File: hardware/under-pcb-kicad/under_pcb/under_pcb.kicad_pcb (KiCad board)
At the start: 2 copper layers, 90 x 160.1 mm, 7 parts, among them J1 Conn_01x08, J2 Conn_01x08, J3 Conn_01x08, J4 Conn_01x06, J5 Conn_02x18_Odd_Even, J6 Conn_01x08, J7 Conn_01x04

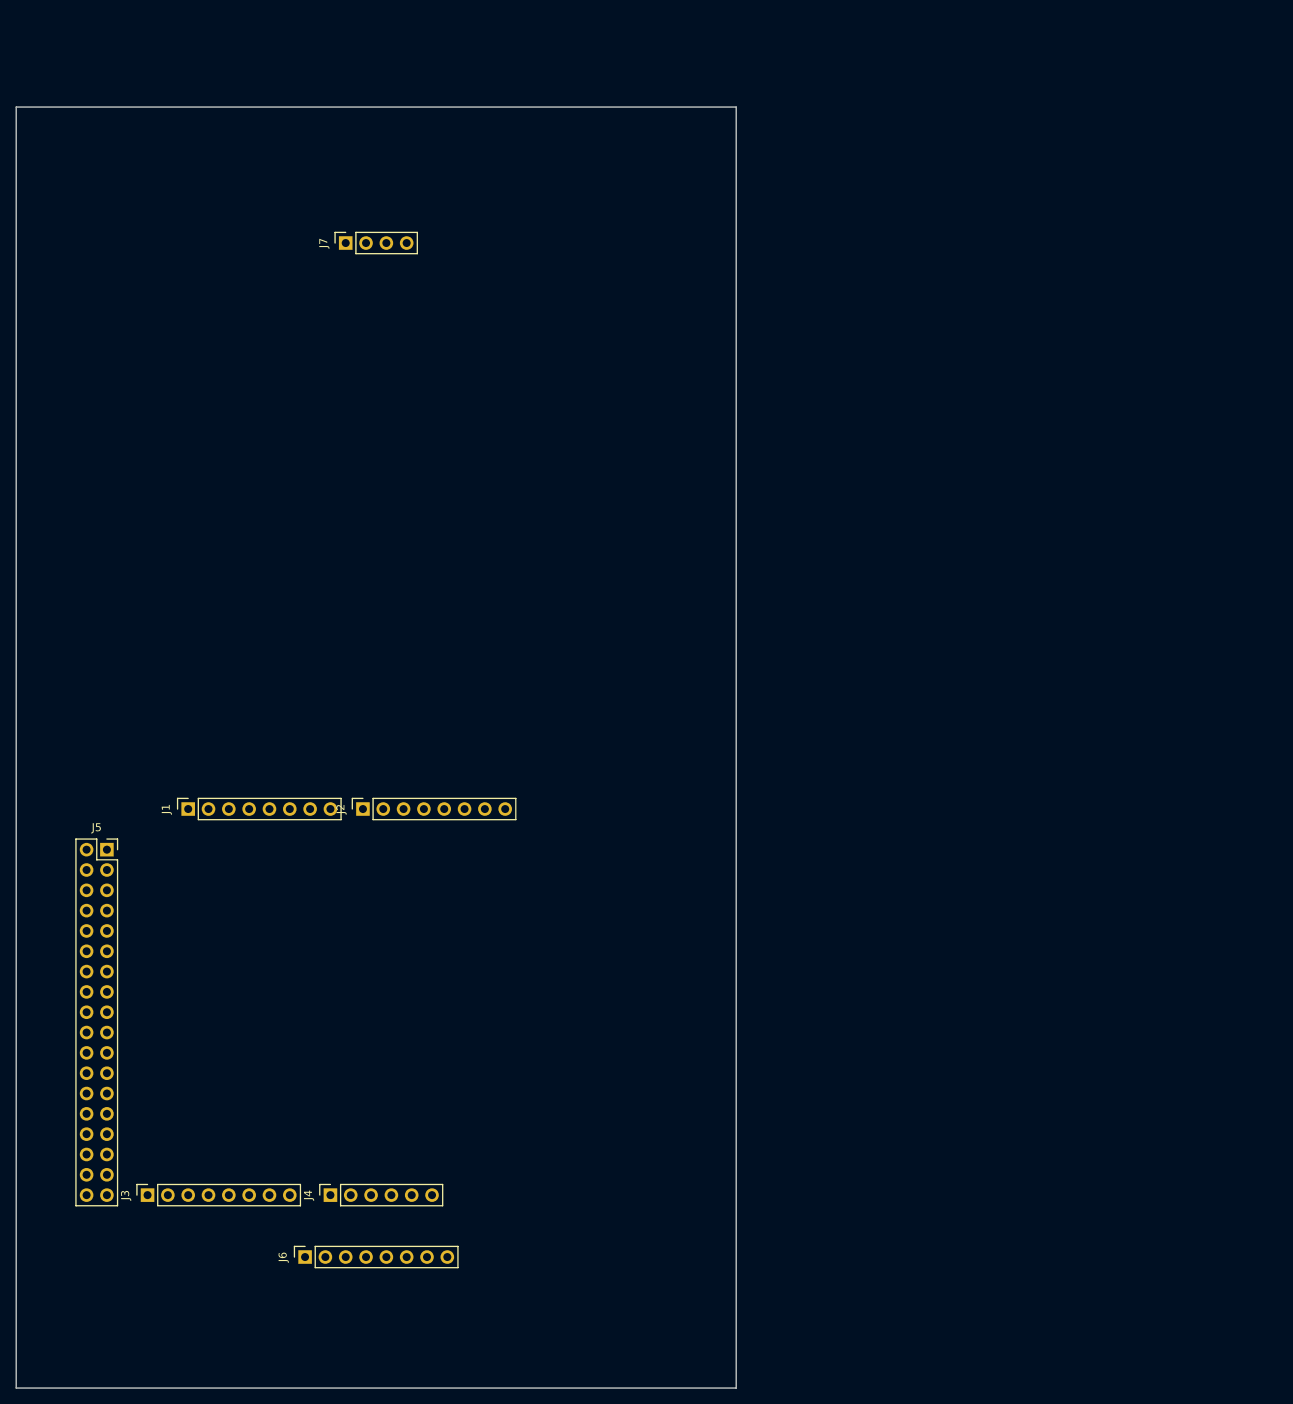
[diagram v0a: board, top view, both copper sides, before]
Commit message: wiring and routing under pcb
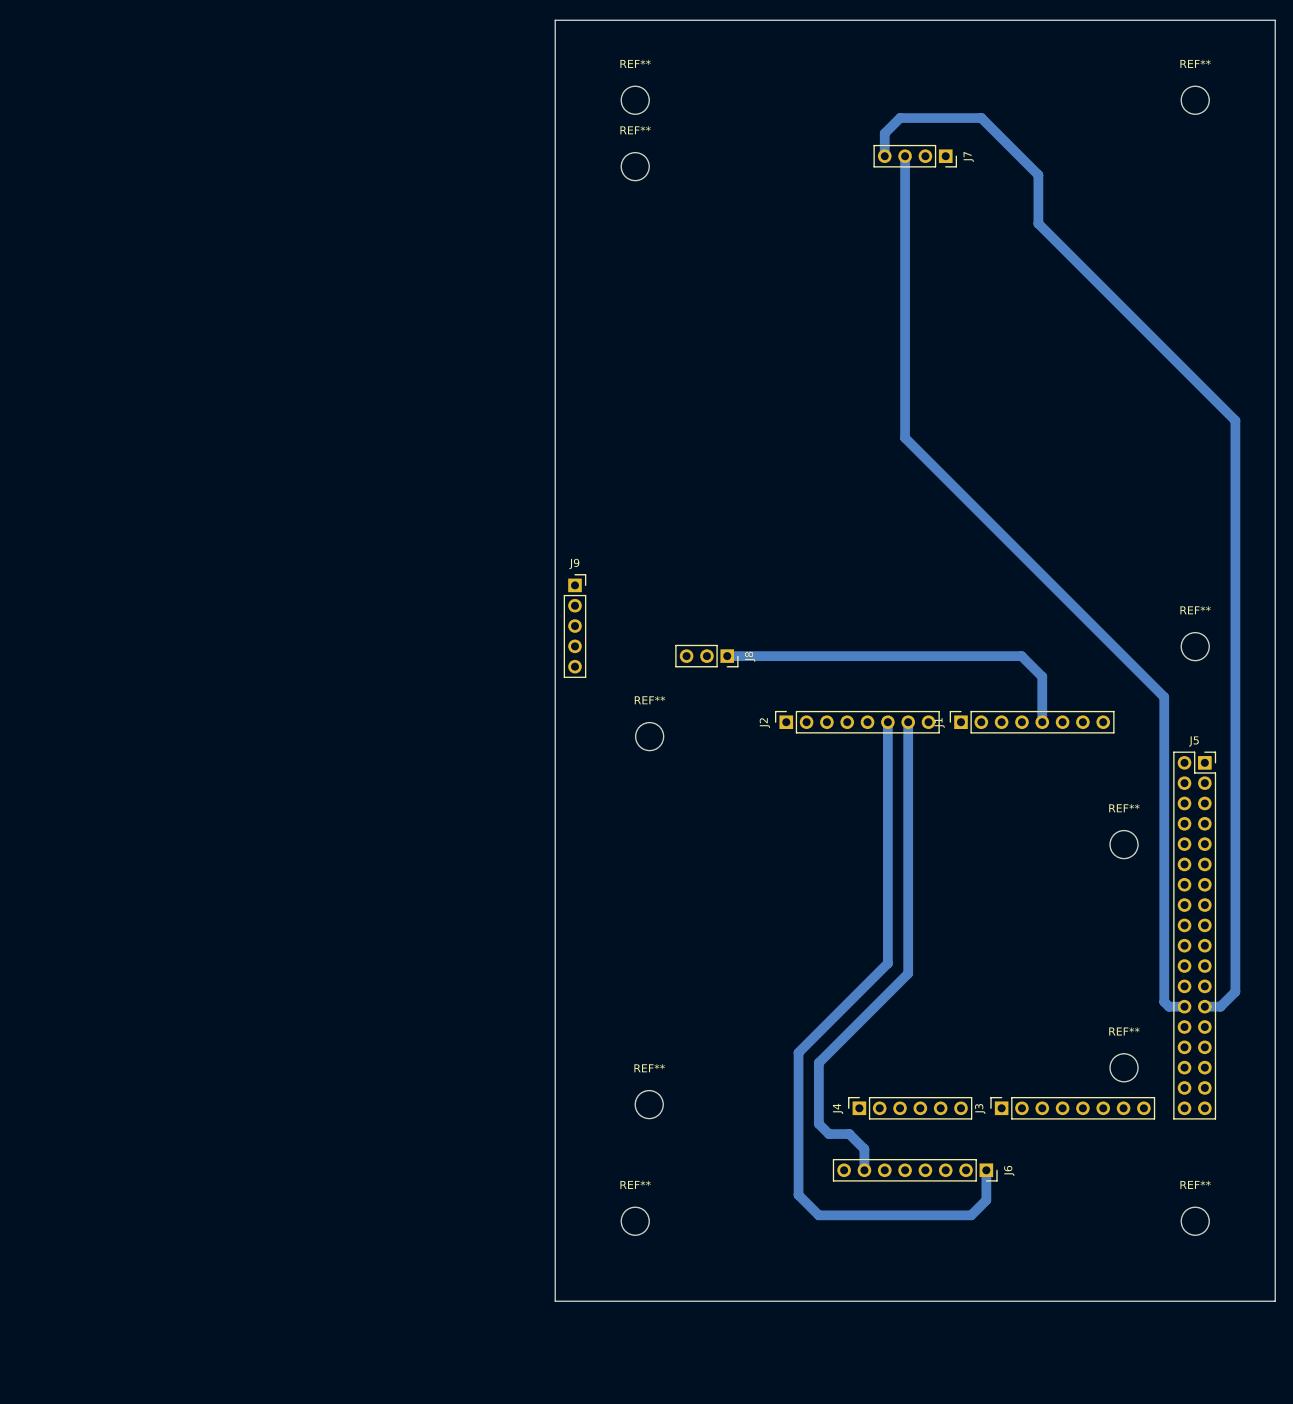
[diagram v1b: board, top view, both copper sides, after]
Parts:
- added J8: Conn_01x03, Connector_PinSocket_2.54mm:PinSocket_1x03_P2.54mm_Vertical, F.Cu at (103.9, 103.5)
- added J9: Conn_01x05, Connector_PinSocket_2.54mm:PinSocket_1x05_P2.54mm_Vertical, F.Cu at (84.8, 94.7)
- added REF**: MountingHole_3.5mm, MountingHole:MountingHole_3.5mm, F.Cu at (162.4, 34.0)
- added REF**: MountingHole_3.5mm, MountingHole:MountingHole_3.5mm, F.Cu at (92.4, 34.0)
- added REF**: MountingHole_3.5mm, MountingHole:MountingHole_3.5mm, F.Cu at (162.4, 174.2)
- added REF**: MountingHole_3.5mm, MountingHole:MountingHole_3.5mm, F.Cu at (92.4, 174.2)
- added REF**: MountingHole_3.5mm, MountingHole:MountingHole_3.5mm, F.Cu at (94.1, 159.6)
- added REF**: MountingHole_3.5mm, MountingHole:MountingHole_3.5mm, F.Cu at (153.5, 155.0)
- added REF**: MountingHole_3.5mm, MountingHole:MountingHole_3.5mm, F.Cu at (153.5, 127.1)
- added REF**: MountingHole_3.5mm, MountingHole:MountingHole_3.5mm, F.Cu at (94.2, 113.6)
- added REF**: MountingHole_3.5mm, MountingHole:MountingHole_3.5mm, F.Cu at (162.4, 102.3)
- added REF**: MountingHole_3.5mm, MountingHole:MountingHole_3.5mm, F.Cu at (92.4, 42.3)
- moved J5 137.7 mm to (163.6, 116.9)
- moved J3 107.3 mm to (138.2, 160.0)
- moved J1 97.2 mm to (133.1, 111.8)
- moved J6 85.8 mm to (136.3, 167.8), turned to 270 degrees
- moved J7 75.8 mm to (131.2, 41.0), turned to 270 degrees
- moved J4 67.0 mm to (120.4, 160.0)
- moved J2 54.0 mm to (111.3, 111.8)
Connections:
- J2 pad 2: Net-(J2-Pad2) -> GND
- J4 pad 2: GND -> Net-(J4-Pad2)
- J4 pad 3: GND -> +5V
- J4 pad 4: +5V -> GND
- J4 pad 5: Net-(J4-Pad5) -> GND
- J5 pad 33: Net-(J5-Pad33) -> GND
- J5 pad 34: Net-(J5-Pad34) -> GND
- J5 pad 35: Net-(J5-Pad35) -> +5V
- J5 pad 36: Net-(J5-Pad36) -> +5V
- J6 pad 1: Net-(J2-Pad3) -> Net-(J2-Pad6)
- J6 pad 2: Net-(J2-Pad6) -> Net-(J2-Pad3)
- J6 pad 3: Net-(J2-Pad4) -> Net-(J2-Pad5)
- J6 pad 4: Net-(J2-Pad5) -> Net-(J2-Pad4)
- J6 pad 7: Net-(J2-Pad2) -> Net-(J2-Pad7)
- J7 pad 1: Net-(J7-Pad1) -> +5V
- J7 pad 2: Net-(J7-Pad2) -> GND
- J7 pad 3: Net-(J7-Pad3) -> Net-(J5-Pad26)
- J7 pad 4: Net-(J7-Pad4) -> Net-(J5-Pad25)
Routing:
- net Net-(J5-Pad25): track 0.00 -> 142.7 mm
- net Net-(J5-Pad26): track 0.00 -> 121.9 mm
- net Net-(J2-Pad6): track 0.00 -> 92.8 mm
- net Net-(J2-Pad7): track 0.00 -> 64.5 mm
- net Net-(J1-Pad5): track 0.00 -> 46.1 mm

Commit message: board routing donr on under_pcb/patty board
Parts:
- added BZ1: Buzzer, Buzzer_Beeper:Buzzer_12x9.5RM7.6, F.Cu at (109.0, 29.8)
- added C1: 0.1uF, Capacitor_THT:C_Disc_D5.0mm_W2.5mm_P2.50mm, F.Cu at (134.5, 153.3)
- added J10: Conn_01x01, Connector_PinSocket_2.54mm:PinSocket_1x01_P2.54mm_Vertical, F.Cu at (146.0, 27.3)
- added J11: Conn_01x01, Connector_PinSocket_2.54mm:PinSocket_1x01_P2.54mm_Vertical, F.Cu at (152.5, 27.3)
- added R1: 100R, Resistor_THT:R_Axial_DIN0207_L6.3mm_D2.5mm_P10.16mm_Horizontal, F.Cu at (125.9, 60.3)
- added R2: 10K, Resistor_THT:R_Axial_DIN0207_L6.3mm_D2.5mm_P10.16mm_Horizontal, F.Cu at (142.7, 72.3)
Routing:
- net +5V: track 0.00 -> 258.4 mm
- net GND: track 0.00 -> 118.0 mm, vias 0 -> 6
- net Net-(J2-Pad3): track 0.00 -> 110.2 mm
- net Net-(J2-Pad4): track 0.00 -> 98.5 mm
- net Net-(J2-Pad5): track 0.00 -> 96.2 mm, vias 0 -> 2
- net Net-(J1-Pad6): track 0.00 -> 87.9 mm, vias 0 -> 4
- net Net-(C1-Pad1): track 0.00 -> 75.6 mm, vias 0 -> 2
- net Net-(J1-Pad3): track 0.00 -> 70.5 mm, vias 0 -> 2
- net Net-(J1-Pad2): track 0.00 -> 70.2 mm, vias 0 -> 2
- net Net-(J1-Pad1): track 0.00 -> 68.0 mm, vias 0 -> 2
- net Net-(J1-Pad4): track 0.00 -> 53.4 mm, vias 0 -> 2
- net Net-(BZ1-Pad1): track 0.00 -> 37.5 mm
- net Net-(J5-Pad26): track 121.9 -> 144.2 mm
- net Net-(J5-Pad25): track 142.7 -> 151.3 mm
- net Net-(J2-Pad7): track 64.5 -> 72.3 mm
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- added copper zone on B.Cu, net GND
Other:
- net class Default: clearance 0.2 -> 0.8128
- rule trace_clearance: 0.2 -> 0.8128
- board text added: "LEADTECH CSPG PATTY BOARD V1.0 20180220"

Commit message: update results, updated patty board
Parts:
- moved J10 3.56 mm to (146.0, 30.9)
- moved J11 3.56 mm to (152.5, 30.9)
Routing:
- net Net-(J2-Pad3): track 110.2 -> 89.1 mm, vias 0 -> 2
- net Net-(J1-Pad6): track 87.9 -> 84.3 mm
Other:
- board size 90 x 160.1 mm -> 90 x 153 mm

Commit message: add supply jumper on OLED for patty board
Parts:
- added J12: Conn_01x01, Connector_PinSocket_2.54mm:PinSocket_1x01_P2.54mm_Vertical, F.Cu at (126.1, 53.4)
- added J13: Conn_01x01, Connector_PinSocket_2.54mm:PinSocket_1x01_P2.54mm_Vertical, F.Cu at (135.0, 49.6)
- added J14: Conn_01x01, Connector_PinSocket_2.54mm:PinSocket_1x01_P2.54mm_Vertical, F.Cu at (126.1, 45.8)
- added J15: Conn_01x01, Connector_PinSocket_2.54mm:PinSocket_1x01_P2.54mm_Vertical, F.Cu at (135.0, 53.4)
- added J16: Conn_01x01, Connector_PinSocket_2.54mm:PinSocket_1x01_P2.54mm_Vertical, F.Cu at (126.1, 49.6)
- added J17: Conn_01x01, Connector_PinSocket_2.54mm:PinSocket_1x01_P2.54mm_Vertical, F.Cu at (135.0, 45.8)
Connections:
- J7 pad 1: +5V -> Net-(J13-Pad1)
- J7 pad 2: GND -> Net-(J16-Pad1)
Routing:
- net GND: track 118.0 -> 146.0 mm, vias 6 -> 8
- net Net-(J13-Pad1): track 0.00 -> 12.4 mm
- net Net-(J16-Pad1): track 0.00 -> 10.8 mm
- net +5V: track 258.4 -> 255.6 mm
- net Net-(C1-Pad1): track 75.6 -> 73.6 mm
- net Net-(J5-Pad26): track 144.2 -> 145.0 mm
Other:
- board text added: "CSPG PATTY BOARD V1.0a"
- board text added: "LEADTECH 20180301"
- board text removed: "LEADTECH CSPG PATTY BOARD V1.0 20180220"
